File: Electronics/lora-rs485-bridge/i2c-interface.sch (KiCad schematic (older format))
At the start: 5 parts

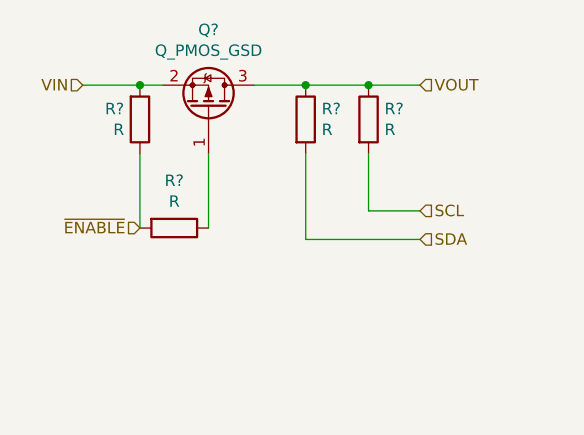
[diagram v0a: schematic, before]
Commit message: Some PCB routing is done
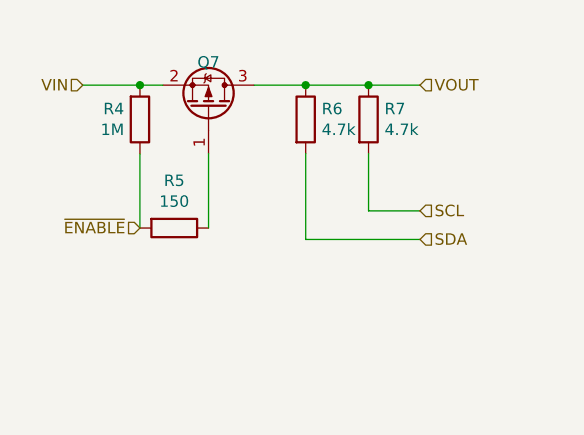
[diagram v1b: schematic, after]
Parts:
- removed Q?: Q_PMOS_GSD, symbol Device:Q_PMOS_GSD
- added Q7: Q_PMOS_GSD, Package_TO_SOT_SMD:SOT-23, symbol Device:Q_PMOS_GSD
- R4: renamed from R?; value R -> 1M; footprint (none) -> Resistor_SMD:R_0603_1608Metric
- R5: renamed from R?; value R -> 150; footprint (none) -> Resistor_SMD:R_0603_1608Metric
- R6, R7: renamed from R?; value R -> 4.7k; footprint (none) -> Resistor_SMD:R_0603_1608Metric
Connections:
- net VIN: now also Q7.2 (S)
- net VOUT: now also Q7.3 (D)
- net at R5.1: now also Q7.1 (G)
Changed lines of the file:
@@
 EESchema Schematic File Version 5
-LIBS:lora-bridge-cache
 EELAYER 30 0
 EELAYER END
 $Descr A4 11693 8268
 encoding utf-8
-Sheet 5 5
+Sheet 4 5
 Title ""
 Date ""
@@
 ~ENABLE
 $Comp
-L Device:R R?
+L Device:R R7
 U 1 1 5D84EABD
 P 5400 2350
-F 0 "R?" H 5470 2396 50  0000 L CNN
-F 1 "R" H 5470 2305 50  0000 L CNN
-F 2 "" V 5330 2350 50  0001 C CNN
+F 0 "R7" H 5470 2396 50  0000 L CNN
+F 1 "4.7k" H 5470 2305 50  0000 L CNN
+F 2 "Resistor_SMD:R_0603_1608Metric" V 5330 2350 50  0001 C CNN
 F 3 "~" H 5400 2350 50  0001 C CNN
 	1    5400 2350
@@
 $EndComp
 $Comp
-L Device:R R?
+L Device:R R6
 U 1 1 5D84F22A
 P 5125 2350
-F 0 "R?" H 5195 2396 50  0000 L CNN
-F 1 "R" H 5195 2305 50  0000 L CNN
-F 2 "" V 5055 2350 50  0001 C CNN
+F 0 "R6" H 5195 2396 50  0000 L CNN
+F 1 "4.7k" H 5195 2305 50  0000 L CNN
+F 2 "Resistor_SMD:R_0603_1608Metric" V 5055 2350 50  0001 C CNN
 F 3 "~" H 5125 2350 50  0001 C CNN
 	1    5125 2350
@@
 Wire Wire Line
 	5125 2875 5625 2875
-$Comp
-L Device:Q_PMOS_GSD Q?
-U 1 1 5D85009B
-P 4700 2300
-F 0 "Q?" V 5042 2300 50  0000 C CNN
-F 1 "Q_PMOS_GSD" V 4951 2300 50  0000 C CNN
-F 2 "" H 4900 2400 50  0001 C CNN
-F 3 "~" H 4700 2300 50  0001 C CNN
-	1    4700 2300
-	0    1    -1   0
-$EndComp
 Wire Wire Line
 	4900 2200 5125 2200
 Connection ~ 5125 2200
 $Comp
-L Device:R R?
+L Device:R R4
 U 1 1 5D8521B9
 P 4400 2350
-F 0 "R?" H 4331 2304 50  0000 R CNN
-F 1 "R" H 4331 2395 50  0000 R CNN
-F 2 "" V 4330 2350 50  0001 C CNN
+F 0 "R4" H 4331 2304 50  0000 R CNN
+F 1 "1M" H 4331 2395 50  0000 R CNN
+F 2 "Resistor_SMD:R_0603_1608Metric" V 4330 2350 50  0001 C CNN
 F 3 "~" H 4400 2350 50  0001 C CNN
 	1    4400 2350
@@
 	4400 2200 4500 2200
 $Comp
-L Device:R R?
+L Device:R R5
 U 1 1 5D853F04
 P 4550 2825
-F 0 "R?" V 4343 2825 50  0000 C CNN
-F 1 "R" V 4434 2825 50  0000 C CNN
-F 2 "" V 4480 2825 50  0001 C CNN
+F 0 "R5" V 4343 2825 50  0000 C CNN
+F 1 "150" V 4434 2825 50  0000 C CNN
+F 2 "Resistor_SMD:R_0603_1608Metric" V 4480 2825 50  0001 C CNN
 F 3 "~" H 4550 2825 50  0001 C CNN
 	1    4550 2825
@@
 	4150 2200 4400 2200
 Connection ~ 4400 2200
+$Comp
+L Device:Q_PMOS_GSD Q7
+U 1 1 57FC85CD
+P 4700 2300
+F 0 "Q7" V 4900 2300 50  0000 C CNN
+F 1 "Q_PMOS_GSD" V 4937 2300 50  0001 C CNN
+F 2 "Package_TO_SOT_SMD:SOT-23" H 4900 2400 29  0001 C CNN
+F 3 "" H 4700 2300 60  0000 C CNN
+F 4 "NX2301P,215 " H 4700 2300 60  0001 C CNN "PartNo"
+F 5 "NXP" H 4700 2300 60  0001 C CNN "Manufacturer"
+F 6 "1894738" H 4700 2300 60  0001 C CNN "Distributor"
+F 7 "Exact as specified" H 4700 2300 50  0001 C CNN "Comment"
+	1    4700 2300
+	0    1    -1   0
+$EndComp
 $EndSCHEMATC

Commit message: Add ESD protection to i2c lines, change VIN TVS diode to higher voltage, add series resistors to SPI lines, compress the PCB to be at width of typical 4xAA battery holder
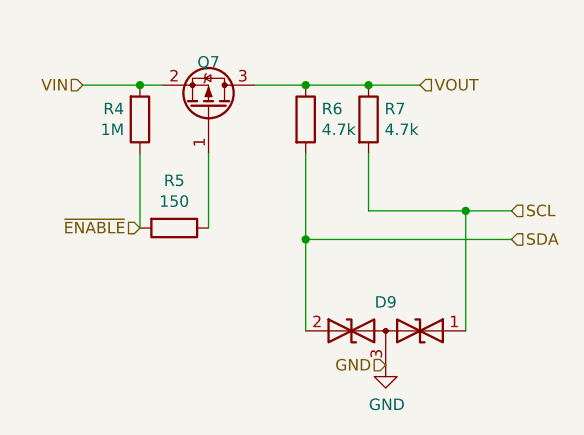
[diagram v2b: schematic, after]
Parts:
- added D9: D_TVS_x2_AAC, miceuz-lib:SC89, symbol Device:D_TVS_x2_AAC
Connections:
- net SCL: now also D9.1 (A1)
- net SDA: now also D9.2 (A2)
- new net GND: D9.3 (common)
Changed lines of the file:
@@
 $Descr A4 11693 8268
 encoding utf-8
-Sheet 4 5
+Sheet 3 5
 Title ""
 Date ""
@@
 Text HLabel 5625 2200 2    50   Input ~ 0
 VOUT
-Text HLabel 5625 2750 2    50   Input ~ 0
+Text HLabel 6025 2750 2    50   Input ~ 0
 SCL
-Text HLabel 5625 2875 2    50   Input ~ 0
+Text HLabel 6025 2875 2    50   Input ~ 0
 SDA
 Text HLabel 4400 2825 0    50   Input ~ 0
@@
 	5400 2500 5400 2750
 Wire Wire Line
-	5400 2750 5625 2750
+	5400 2750 5825 2750
 Wire Wire Line
 	5125 2500 5125 2875
 Wire Wire Line
-	5125 2875 5625 2875
+	5125 2875 6025 2875
 Wire Wire Line
 	4900 2200 5125 2200
@@
 	0    1    -1   0
 $EndComp
+$Comp
+L Device:D_TVS_x2_AAC D9
+U 1 1 5CF95011
+P 5475 3275
+F 0 "D9" H 5475 3400 50  0000 C CNN
+F 1 "D_TVS_x2_AAC" H 5475 3400 50  0001 C CNN
+F 2 "miceuz-lib:SC89" H 5325 3275 50  0001 C CNN
+F 3 "~" H 5325 3275 50  0001 C CNN
+F 4 "ON SEMICONDUCTOR" H 3425 1575 50  0001 C CNN "Manufacturer"
+F 5 " NZL5V6AXV3T1G" H 3425 1575 50  0001 C CNN "PartNo"
+	1    5475 3275
+	-1   0    0    -1
+$EndComp
+Wire Wire Line
+	5125 2875 5125 3275
+Connection ~ 5125 2875
+Wire Wire Line
+	5825 2750 5825 3275
+Connection ~ 5825 2750
+Wire Wire Line
+	5825 2750 6025 2750
+$Comp
+L power:GND #PWR0137
+U 1 1 5DAF890B
+P 5475 3425
+F 0 "#PWR0137" H 5475 3175 50  0001 C CNN
+F 1 "GND" H 5480 3252 50  0000 C CNN
+F 2 "" H 5475 3425 50  0001 C CNN
+F 3 "" H 5475 3425 50  0001 C CNN
+	1    5475 3425
+	1    0    0    -1
+$EndComp
+Text HLabel 5475 3425 0    50   Input ~ 0
+GND
 $EndSCHEMATC
